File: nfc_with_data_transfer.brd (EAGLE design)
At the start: 15.4 x 25.1 mm, 6 parts

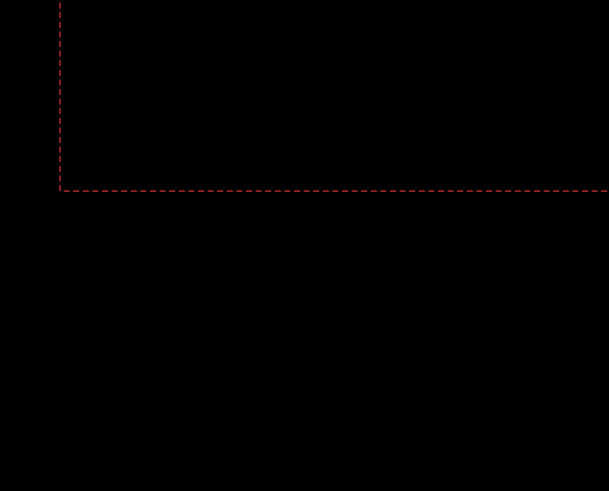
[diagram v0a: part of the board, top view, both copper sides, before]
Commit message: Added suggested resistors
Added 4k7 pull-up resistors on SCL and SDA pins. Also added 10 kOhm pull-up resistor on Field Detection line.
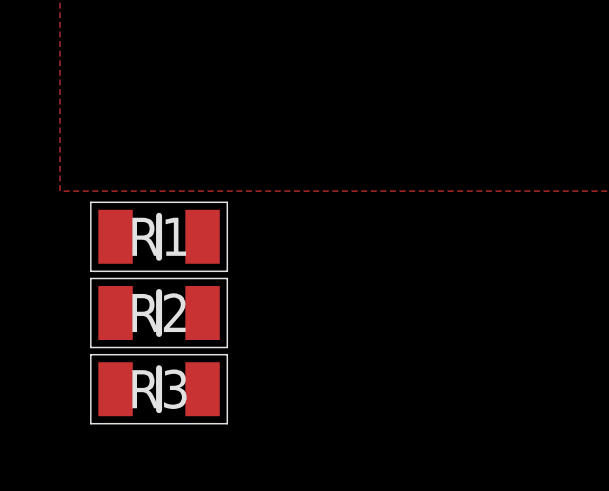
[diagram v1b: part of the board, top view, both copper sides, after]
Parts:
- added R1, R2: KTR18EZPF4701, KTR18EZPF4701:RESC3216X65N
- added R3: KTR18EZPF1002, KTR18EZPF1002:RESC3216X65N
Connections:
- removed net VCC: U1.6
- new net COIL: U1.1, U1.8
- new net N$2: R3.1, U1.4
- net 2.8V: now also R1.2, R2.2, R3.2, U1.6
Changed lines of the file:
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@@
 <element name="U1" library="AlterNail" package="NT3H1101" value="" x="13.97" y="15.24"/>
 <element name="C1" library="SparkFun-Capacitors" package="1206" value="0.2uf" x="13.97" y="18.288"/>
+<element name="R1" library="KTR18EZPF4701" package="RESC3216X65N" value="KTR18EZPF4701" x="-4.318" y="-10.414">
+<attribute name="3D_PACKAGE" value="" x="-4.318" y="-10.414" size="1.778" layer="27" display="off"/>
+<attribute name="MANUFACTURER_PART_NUMBER" value="KTR18EZPF4701" x="-4.318" y="-10.414" size="1.778" layer="27" display="off"/>
+<attribute name="MANUFACTURER_NAME" value="ROHM Semiconductor" x="-4.318" y="-10.414" size="1.778" layer="27" display="off"/>
+<attribute name="HEIGHT" value="0.65mm" x="-4.318" y="-10.414" size="1.778" layer="27" display="off"/>
+<attribute name="DESCRIPTION" value="Thick Film Resistors - SMD 1206 4K7ohm 1% High VoltageAEC-Q200" x="-4.318" y="-10.414" size="1.778" layer="27" display="off"/>
+</element>
+<element name="R2" library="KTR18EZPF4701" package="RESC3216X65N" value="KTR18EZPF4701" x="-4.318" y="-12.954">
+<attribute name="3D_PACKAGE" value="" x="-4.318" y="-12.954" size="1.778" layer="27" display="off"/>
+<attribute name="MANUFACTURER_PART_NUMBER" value="KTR18EZPF4701" x="-4.318" y="-12.954" size="1.778" layer="27" display="off"/>
+<attribute name="MANUFACTURER_NAME" value="ROHM Semiconductor" x="-4.318" y="-12.954" size="1.778" layer="27" display="off"/>
+<attribute name="HEIGHT" value="0.65mm" x="-4.318" y="-12.954" size="1.778" layer="27" display="off"/>
+<attribute name="DESCRIPTION" value="Thick Film Resistors - SMD 1206 4K7ohm 1% High VoltageAEC-Q200" x="-4.318" y="-12.954" size="1.778" layer="27" display="off"/>
+</element>
+<element name="R3" library="KTR18EZPF1002" package="RESC3216X65N" value="KTR18EZPF1002" x="-4.318" y="-15.494">
+<attribute name="3D_PACKAGE" value="" x="-4.318" y="-15.494" size="1.778" layer="27" display="off"/>
+<attribute name="MANUFACTURER_PART_NUMBER" value="KTR18EZPF1002" x="-4.318" y="-15.494" size="1.778" layer="27" display="off"/>
+<attribute name="MANUFACTURER_NAME" value="ROHM Semiconductor" x="-4.318" y="-15.494" size="1.778" layer="27" display="off"/>
+<attribute name="HEIGHT" value="0.65mm" x="-4.318" y="-15.494" size="1.778" layer="27" display="off"/>
+<attribute name="DESCRIPTION" value="Thick Film Resistors - SMD 1206 10Kohm 1% High VoltageAEC-Q200" x="-4.318" y="-15.494" size="1.778" layer="27" display="off"/>
+</element>
 </elements>
 <signals>
@@
 <contactref element="U1" pad="7"/>
 <contactref element="C1" pad="1"/>
-<wire x1="9.906" y1="18.542" x2="16.145" y2="15.565" width="0" layer="19" extent="1-16"/>
+<contactref element="U1" pad="6"/>
+<contactref element="R2" pad="2"/>
+<contactref element="R1" pad="2"/>
+<contactref element="R3" pad="2"/>
+<wire x1="16.145" y1="14.915" x2="16.145" y2="15.565" width="0" layer="19" extent="1-1"/>
+<wire x1="12.57" y1="18.288" x2="16.145" y2="15.565" width="0" layer="19" extent="1-1"/>
+<wire x1="9.906" y1="18.542" x2="12.57" y2="18.288" width="0" layer="19" extent="1-16"/>
 <wire x1="6.416" y1="22.034" x2="8.89" y2="22.352" width="0" layer="19" extent="1-1"/>
 <wire x1="5.121" y1="19.109" x2="6.416" y2="22.034" width="0" layer="19" extent="1-1"/>
-<wire x1="12.57" y1="18.288" x2="9.017" y2="9.3472" width="0" layer="19" extent="1-1"/>
-</signal>
-<signal name="VCC">
-<contactref element="U1" pad="6"/>
+<wire x1="-2.868" y1="-10.414" x2="9.017" y2="9.3472" width="0" layer="19" extent="1-1"/>
+<wire x1="-2.868" y1="-12.954" x2="-2.868" y2="-10.414" width="0" layer="19" extent="1-1"/>
+<wire x1="-2.868" y1="-15.494" x2="-2.868" y2="-12.954" width="0" layer="19" extent="1-1"/>
 </signal>
 <signal name="DATA">
@@
 <wire x1="9.398" y1="6.858" x2="9.398" y2="5.9944" width="0.3048" layer="1"/>
 </signal>
+<signal name="COIL">
+<contactref element="U1" pad="8"/>
+<contactref element="U1" pad="1"/>
+<wire x1="11.795" y1="16.215" x2="16.145" y2="16.215" width="0" layer="19" extent="1-1"/>
+</signal>
+<signal name="N$2">
+<contactref element="U1" pad="4"/>
+<contactref element="R3" pad="1"/>
+<wire x1="-5.768" y1="-15.494" x2="11.795" y2="14.265" width="0" layer="19" extent="1-1"/>
+</signal>
 </signals>
